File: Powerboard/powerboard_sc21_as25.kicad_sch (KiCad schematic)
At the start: 43 parts

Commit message: 1
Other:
- removed sheet Battery Monitor
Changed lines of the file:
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@@
-    )
-  )
-  (sheet (at 87.63 167.005) (size 25.146 18.796) (fields_autoplaced)
-    (stroke (width 0.1524) (type solid) (color 0 0 0 0))
-    (fill (color 0 0 0 0.0000))
-    (property "Sheet name" "Battery Monitor" (id 0) (at 87.63 166.2934 0)
-      (effects (font (size 1.27 1.27)) (justify left bottom))
-    )
-    (property "Sheet file" "battmonitor.kicad_sch" (id 1) (at 87.63 186.3856 0)
-      (effects (font (size 1.27 1.27)) (justify left top))
     )
   )
@@
     (path "/00000000-0000-0000-0000-000061f04c1a" (page "3"))
     (path "/b1853ee1-af2e-49ab-93e4-e29b2d9f793d" (page "4"))
-    (path "/33e9abb9-e634-4336-bd82-f9f25ebb0731" (page "5"))
   )
   (symbol_instances
@@
       (reference "IC?") (unit 1) (value "CP2102") (footprint "QFN50P500X500X100-29N-D")
     )
-    (path "/33e9abb9-e634-4336-bd82-f9f25ebb0731/c1d61362-65a2-49c7-92c4-42116f69f186"
-      (reference "IC?") (unit 1) (value "BQ34Z110PWR") (footprint "SOP65P640X120-14N")
-    )
     (path "/00000000-0000-0000-0000-000061beb629/00000000-0000-0000-0000-000061c1bdf7"

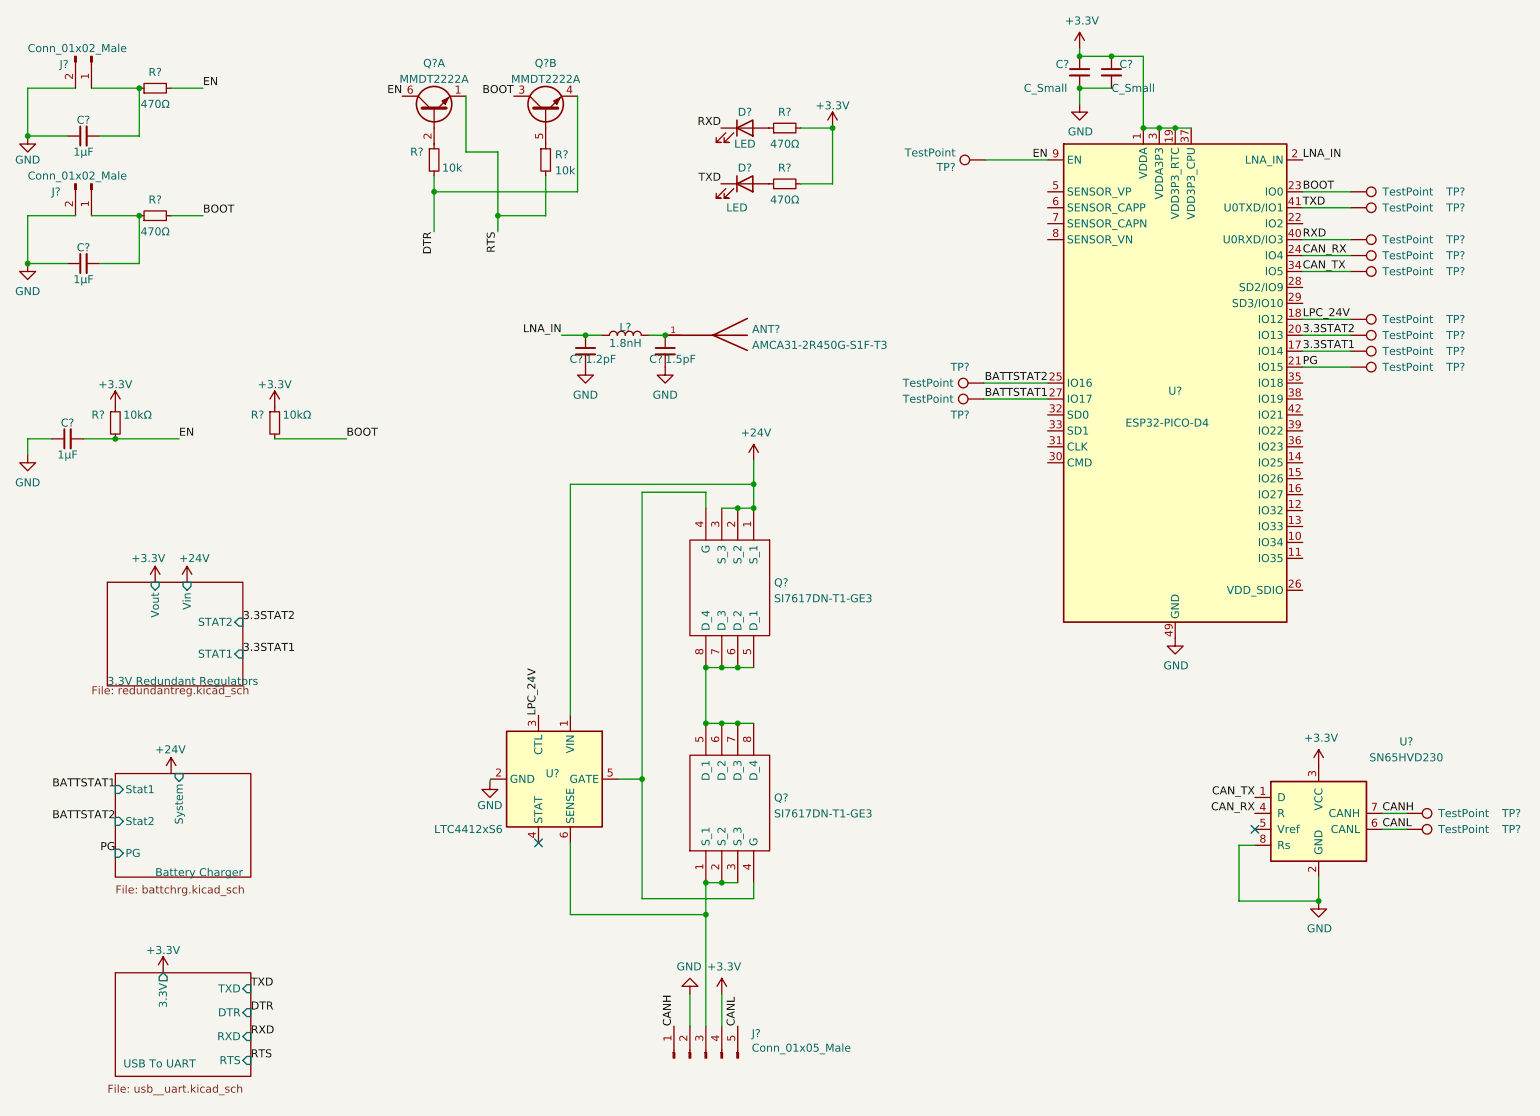
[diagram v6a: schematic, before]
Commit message: Added connectors and potential divider for charge measurement
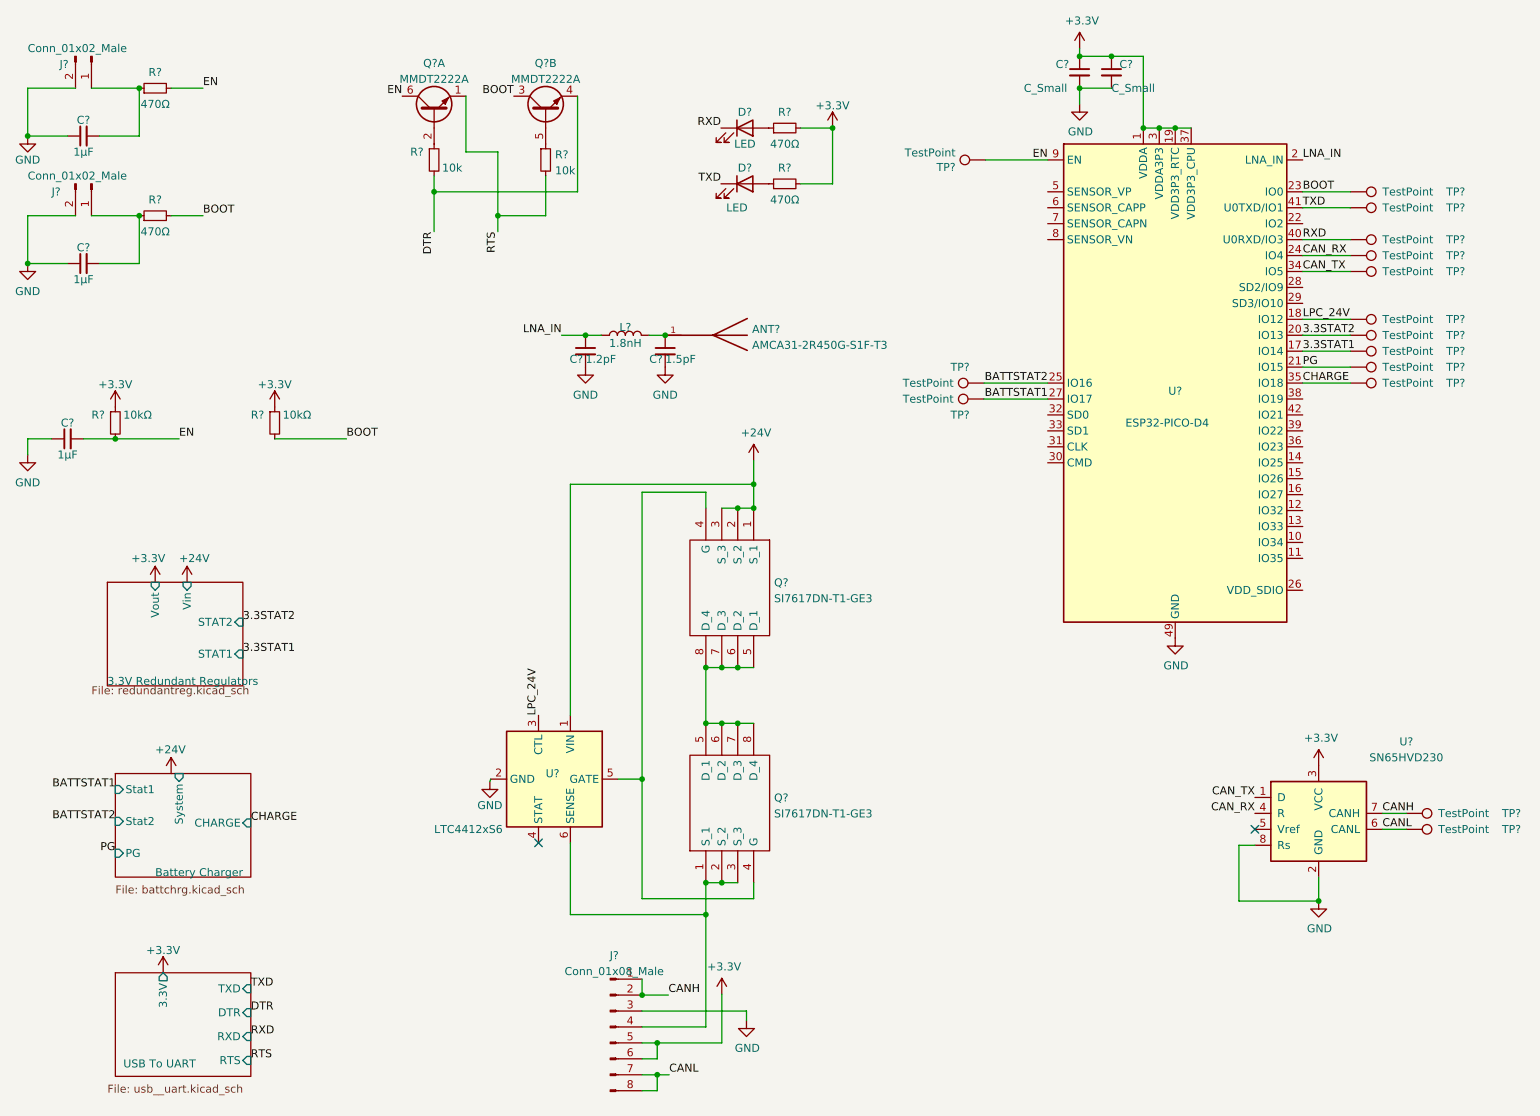
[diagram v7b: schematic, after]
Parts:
- removed J?: Conn_01x05_Male, symbol Connector:Conn_01x05_Male
- added J?: Conn_01x08_Male, Connector_Molex:Molex_Mini-Fit_Jr_5569-16A1_2x08_P4.20mm_Horizontal, symbol Connector:Conn_01x08_Male
- added TP?: TestPoint, symbol Connector:TestPoint
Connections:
- net +3V3: now also J?.5 (Pin_5), J?.6 (Pin_6)
- net CANH: now also J?.1 (Pin_1), J?.2 (Pin_2)
- net CANL: now also J?.7 (Pin_7), J?.8 (Pin_8)
- net GND: now also J?.3 (Pin_3)
- net CHARGE: now reaches U?.35 (IO18)
- net CHARGE: now also TP?.1
- net at Q?.1 (S_1), Q?.2 (S_2), Q?.3 (S_3)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: now also J?.4 (Pin_4)
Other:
- sheet Battery Charger ports: added CHARGE; removed none

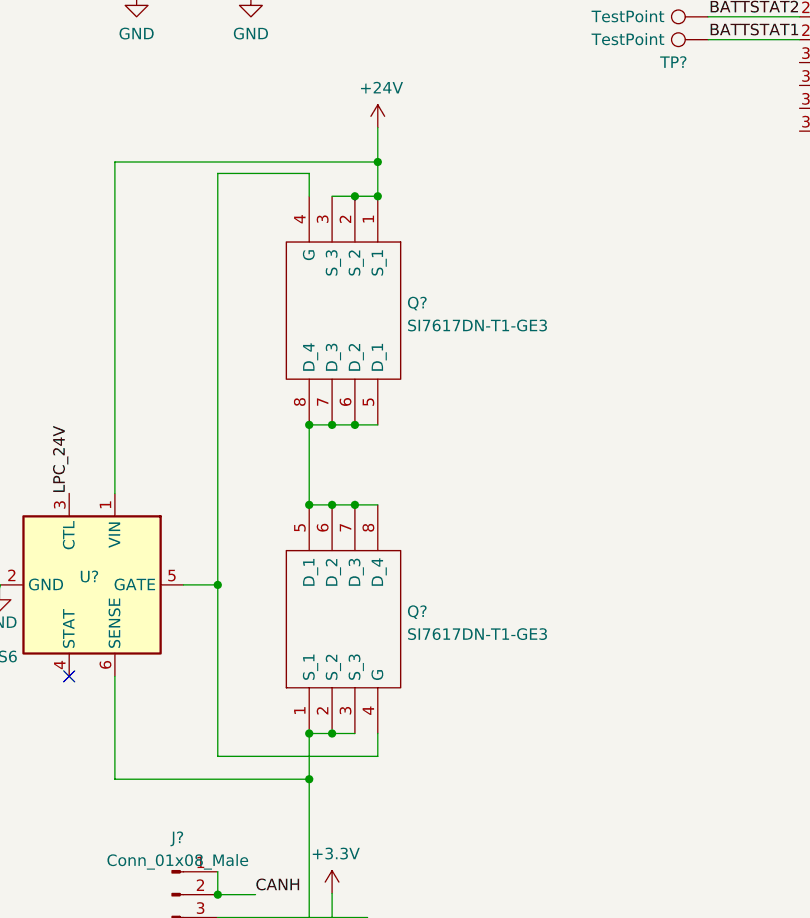
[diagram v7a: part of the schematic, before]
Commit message: Swapped remaining p mosfets
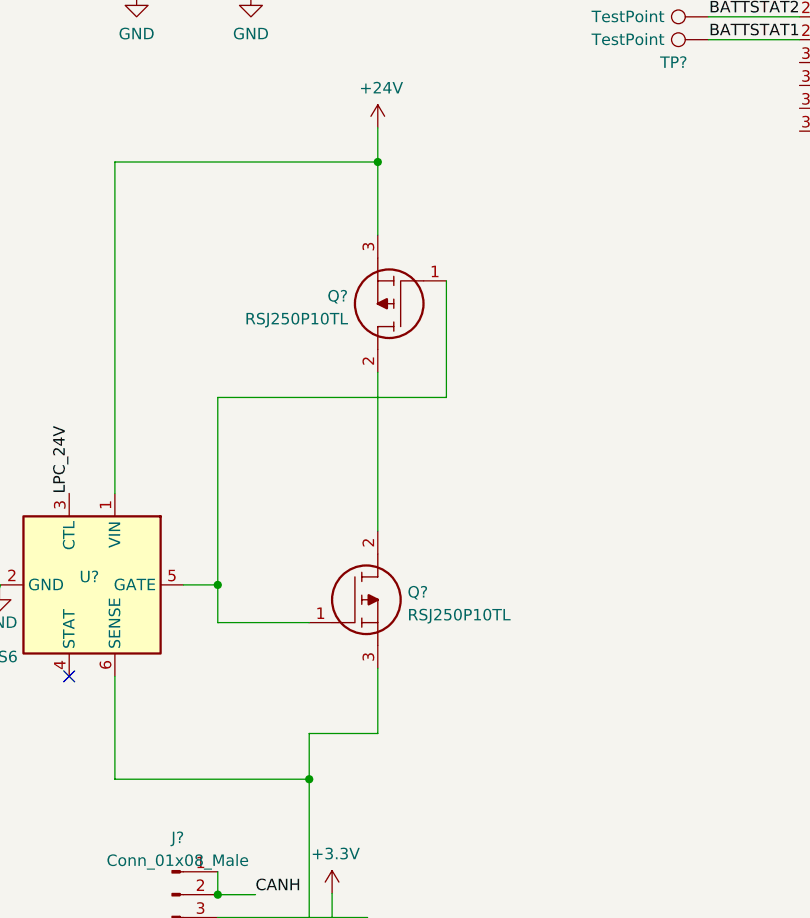
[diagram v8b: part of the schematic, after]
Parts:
- removed Q? (x2): SI7617DN-T1-GE3, SIS862DNT1GE3, symbol iclr:SI7617DN-T1-GE3
- added Q? (x2): RSJ250P10TL, RSJ151P10TL, symbol iclr:RSJ250P10TL
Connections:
- net +24V: now also Q?.3
- net at U?.5 (GATE): now also Q?.1, Q?.1
- net at J?.4 (Pin_4), U?.6 (SENSE): now also Q?.3
- new net: Q?.2, Q?.2
